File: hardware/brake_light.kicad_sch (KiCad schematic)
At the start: 4 parts, among them Q5 PMV450ENEA

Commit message: Add the Cube project
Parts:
- R?: Case 0603 -> (none)
- R?: value R_Small -> 10k
- R?: value R_Small -> 100R
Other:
- note removed: "TODO: Add a mosfet driver"
- moved on the sheet: Q5, R?
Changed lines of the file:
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@@
   (paper "A4")
   (title_block
-    (date "2023-06-06")
+    (date "2023-07-01")
     (rev "${REVISION}")
     (company "Author: I. Kajdan")
     (comment 1 "Reviewer:")
   )
-  (junction (at 153.67 100.33) (diameter 0) (color 0 0 0 0)
+  (junction (at 151.13 110.49) (diameter 0) (color 0 0 0 0)
   )
-  (junction (at 143.51 92.71) (diameter 0) (color 0 0 0 0)
+  (junction (at 140.97 102.87) (diameter 0) (color 0 0 0 0)
   )
-  (wire (pts (xy 135.89 92.71) (xy 133.35 92.71))
+  (wire (pts (xy 133.35 102.87) (xy 130.81 102.87))
     (stroke (width 0) (type default))
   )
-  (wire (pts (xy 153.67 104.14) (xy 153.67 100.33))
+  (wire (pts (xy 151.13 114.3) (xy 151.13 110.49))
     (stroke (width 0) (type default))
   )
-  (wire (pts (xy 143.51 100.33) (xy 146.05 100.33))
+  (wire (pts (xy 140.97 110.49) (xy 143.51 110.49))
     (stroke (width 0) (type default))
   )
-  (wire (pts (xy 143.51 100.33) (xy 143.51 92.71))
+  (wire (pts (xy 140.97 110.49) (xy 140.97 102.87))
     (stroke (width 0) (type default))
   )
-  (wire (pts (xy 140.97 92.71) (xy 143.51 92.71))
+  (wire (pts (xy 138.43 102.87) (xy 140.97 102.87))
     (stroke (width 0) (type default))
   )
-  (wire (pts (xy 153.67 100.33) (xy 153.67 97.79))
+  (wire (pts (xy 151.13 110.49) (xy 151.13 107.95))
     (stroke (width 0) (type default))
   )
-  (wire (pts (xy 153.67 83.82) (xy 153.67 87.63))
+  (wire (pts (xy 151.13 96.52) (xy 151.13 97.79))
     (stroke (width 0) (type default))
   )
-  (wire (pts (xy 143.51 92.71) (xy 146.05 92.71))
+  (wire (pts (xy 140.97 102.87) (xy 143.51 102.87))
     (stroke (width 0) (type default))
   )
-  (wire (pts (xy 153.67 74.93) (xy 153.67 78.74))
+  (wire (pts (xy 151.13 88.9) (xy 151.13 91.44))
     (stroke (width 0) (type default))
   )
-  (wire (pts (xy 151.13 100.33) (xy 153.67 100.33))
+  (wire (pts (xy 148.59 110.49) (xy 151.13 110.49))
     (stroke (width 0) (type default))
   )
-  (wire (pts (xy 157.48 74.93) (xy 153.67 74.93))
+  (wire (pts (xy 154.94 88.9) (xy 151.13 88.9))
     (stroke (width 0) (type default))
   )
-  (text "TODO: Add a mosfet driver" (at 139.7 124.46 0)
-    (effects (font (size 1.27 1.27)) (justify left bottom))
-  )
-  (hierarchical_label "OUT" (shape output) (at 157.48 74.93 0) (fields_autoplaced)
+  (hierarchical_label "OUT" (shape output) (at 154.94 88.9 0) (fields_autoplaced)
     (effects (font (size 1.27 1.27)) (justify left))
   )
-  (hierarchical_label "IN" (shape input) (at 133.35 92.71 180) (fields_autoplaced)
+  (hierarchical_label "IN" (shape input) (at 130.81 102.87 180) (fields_autoplaced)
     (effects (font (size 1.27 1.27)) (justify right))
   )
-  (symbol (lib_id "Simulation_SPICE:NMOS") (at 151.13 92.71 0) (unit 1)
+  (symbol (lib_id "Simulation_SPICE:NMOS") (at 148.59 102.87 0) (unit 1)
     (in_bom yes) (on_board yes) (dnp no)
-    (property "Reference" "Q5" (at 157.48 91.44 0)
+    (property "Reference" "Q5" (at 153.67 101.6 0)
       (effects (font (size 1.27 1.27)) (justify left))
     )
-    (property "Value" "PMV450ENEA" (at 157.48 93.98 0)
+    (property "Value" "PMV450ENEA" (at 153.67 104.14 0)
       (effects (font (size 1.27 1.27)) (justify left))
     )
-    (property "Footprint" "" (at 156.21 90.17 0)
+    (property "Footprint" "" (at 153.67 100.33 0)
       (effects (font (size 1.27 1.27)) hide)
     )
-    (property "Datasheet" "https://assets.nexperia.com/documents/data-sheet/PMV450ENEA.pdf" (at 151.13 105.41 0)
+    (property "Datasheet" "https://assets.nexperia.com/documents/data-sheet/PMV450ENEA.pdf" (at 148.59 115.57 0)
       (effects (font (size 1.27 1.27)) hide)
     )
@@
     )
   )
-  (symbol (lib_id "Device:R_Small") (at 153.67 81.28 0) (unit 1)
+  (symbol (lib_id "Device:R_Small") (at 151.13 93.98 0) (unit 1)
     (in_bom yes) (on_board yes) (dnp no)
-    (property "Reference" "R?" (at 156.4386 78.8416 0)
+    (property "Reference" "R?" (at 152.6286 92.8116 0)
       (effects (font (size 1.27 1.27)) (justify left))
     )
-    (property "Value" "0R" (at 156.4386 81.153 0)
+    (property "Value" "0R" (at 152.6286 95.123 0)
       (effects (font (size 1.27 1.27)) (justify left))
     )
-    (property "Footprint" "Resistor_SMD:R_0603_1608Metric" (at 153.67 81.28 0)
+    (property "Footprint" "Resistor_SMD:R_0603_1608Metric" (at 151.13 93.98 0)
       (effects (font (size 1.27 1.27)) hide)
     )
-    (property "Datasheet" "~" (at 153.67 81.28 0)
+    (property "Datasheet" "~" (at 151.13 93.98 0)
       (effects (font (size 1.27 1.27)) hide)
-    )
-    (property "Case" "0603" (at 156.4386 83.82 0)
-      (effects (font (size 1.27 1.27)) (justify left))
     )
     (pin "1")
@@
     )
   )
-  (symbol (lib_id "Device:R_Small") (at 148.59 100.33 270) (unit 1)
+  (symbol (lib_id "Device:R_Small") (at 146.05 110.49 270) (unit 1)
     (in_bom yes) (on_board yes) (dnp no)
-    (property "Reference" "R?" (at 148.59 97.79 90)
+    (property "Reference" "R?" (at 146.05 107.95 90)
       (effects (font (size 1.27 1.27)))
     )
-    (property "Value" "R_Small" (at 148.59 102.87 90)
+    (property "Value" "10k" (at 146.05 113.03 90)
       (effects (font (size 1.27 1.27)))
     )
-    (property "Footprint" "Resistor_SMD:R_0402_1005Metric" (at 148.59 100.33 0)
+    (property "Footprint" "Resistor_SMD:R_0402_1005Metric" (at 146.05 110.49 0)
       (effects (font (size 1.27 1.27)) hide)
     )
-    (property "Datasheet" "~" (at 148.59 100.33 0)
+    (property "Datasheet" "~" (at 146.05 110.49 0)
       (effects (font (size 1.27 1.27)) hide)
     )
@@
     )
   )
-  (symbol (lib_id "power:GND") (at 153.67 104.14 0) (unit 1)
+  (symbol (lib_id "power:GND") (at 151.13 114.3 0) (unit 1)
     (in_bom yes) (on_board yes) (dnp no)
-    (property "Reference" "#PWR?" (at 153.67 110.49 0)
+    (property "Reference" "#PWR?" (at 151.13 120.65 0)
       (effects (font (size 1.27 1.27)) hide)
     )
-    (property "Value" "GND" (at 153.797 108.5342 0)
+    (property "Value" "GND" (at 151.257 118.6942 0)
       (effects (font (size 1.27 1.27)))
     )
-    (property "Footprint" "" (at 153.67 104.14 0)
+    (property "Footprint" "" (at 151.13 114.3 0)
       (effects (font (size 1.27 1.27)) hide)
     )
-    (property "Datasheet" "" (at 153.67 104.14 0)
+    (property "Datasheet" "" (at 151.13 114.3 0)
       (effects (font (size 1.27 1.27)) hide)
     )
@@
     )
   )
-  (symbol (lib_id "Device:R_Small") (at 138.43 92.71 270) (unit 1)
+  (symbol (lib_id "Device:R_Small") (at 135.89 102.87 270) (unit 1)
     (in_bom yes) (on_board yes) (dnp no)
-    (property "Reference" "R?" (at 138.43 90.17 90)
+    (property "Reference" "R?" (at 135.89 100.33 90)
       (effects (font (size 1.27 1.27)))
     )
-    (property "Value" "R_Small" (at 142.113 95.0214 90)
+    (property "Value" "100R" (at 138.303 105.1814 90)
       (effects (font (size 1.27 1.27)) (justify right))
     )
-    (property "Footprint" "Resistor_SMD:R_0402_1005Metric" (at 138.43 92.71 0)
+    (property "Footprint" "Resistor_SMD:R_0402_1005Metric" (at 135.89 102.87 0)
       (effects (font (size 1.27 1.27)) hide)
     )
-    (property "Datasheet" "~" (at 138.43 92.71 0)
+    (property "Datasheet" "~" (at 135.89 102.87 0)
       (effects (font (size 1.27 1.27)) hide)
     )

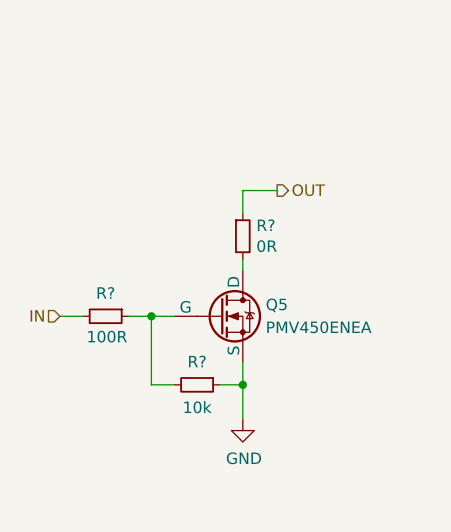
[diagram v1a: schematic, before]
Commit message: Improve the schematic
- add anti-aliasing filters
- rearrange the main connector signals
- improve the power filtering
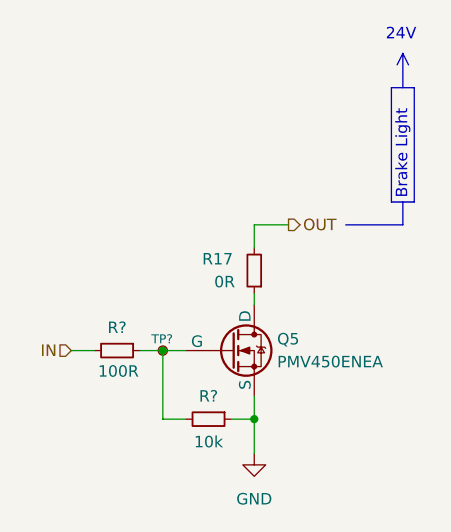
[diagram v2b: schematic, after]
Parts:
- removed R?: 0R, Resistor_SMD:R_0603_1608Metric, symbol Device:R_Small
- added R17: 0R, Resistor_SMD:R_0603_1608Metric, symbol Device:R_Small
- added TP?: TestPoint_Small, TestPoint:TestPoint_Pad_D1.0mm, symbol Connector:TestPoint_Small
- R? (x2): footprint Resistor_SMD:R_0402_1005Metric -> Resistor_SMD:R_0603_1608Metric
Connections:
- net OUT: now also R17.2
- net at Q5.1 (D): now also R17.1
- net at Q5.2 (G), R?.1, R?.2: now also TP?.1
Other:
- note added: "24V"
- note added: "Brake Light"
- moved on the sheet: Q5, R?

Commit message: Set component values
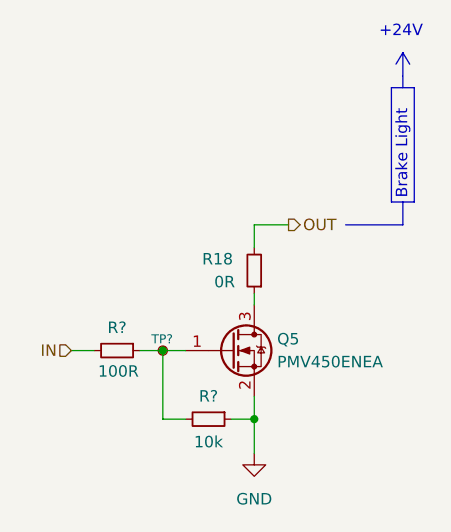
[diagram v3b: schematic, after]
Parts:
- Q5: symbol Simulation_SPICE:NMOS -> Device:Q_NMOS_GSD
- renumbered R17 to R18
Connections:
- net GND: now also Q5.2 (S); no longer Q5.3 (S)
- net at Q5.1 (G): now also R?.1, R?.2, TP?.1; no longer R18.1
- new net: Q5.3 (D), R18.1
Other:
- note added: "+24V"
- note removed: "24V"
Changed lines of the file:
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@@
     (stroke (width 0) (type default))
   )
-  (polyline (pts (xy 168.91 73.66) (xy 168.91 77.47))
+  (polyline (pts (xy 168.148 74.8538) (xy 168.91 73.5838))
     (stroke (width 0) (type default))
   )
@@
     (stroke (width 0) (type default))
   )
+  (polyline (pts (xy 168.91 73.5838) (xy 168.91 76.1492))
+    (stroke (width 0) (type default))
+  )
   (wire (pts (xy 142.24 114.3) (xy 142.24 106.68))
     (stroke (width 0) (type default))
   )
-  (polyline (pts (xy 168.275 74.93) (xy 168.91 73.66))
-    (stroke (width 0) (type default))
-  )
   (wire (pts (xy 139.7 106.68) (xy 142.24 106.68))
     (stroke (width 0) (type default))
@@
     (stroke (width 0) (type default))
   )
+  (polyline (pts (xy 169.672 74.8538) (xy 168.91 73.5838))
+    (stroke (width 0) (type default))
+  )
+  (polyline (pts (xy 168.91 76.2) (xy 168.91 77.47))
+    (stroke (width 0) (type default))
+  )
   (wire (pts (xy 142.24 106.68) (xy 144.78 106.68))
     (stroke (width 0) (type default))
@@
     (stroke (width 0) (type default))
   )
-  (polyline (pts (xy 168.91 73.66) (xy 169.545 74.93))
-    (stroke (width 0) (type default))
-  )
   (wire (pts (xy 156.21 92.71) (xy 152.4 92.71))
     (stroke (width 0) (type default))
-  )
-  (text "24V" (at 167.005 72.39 0)
-    (effects (font (size 1.27 1.27)) (justify left bottom))
   )
   (text "Brake Light" (at 169.545 89.916 90)
     (effects (font (size 1.27 1.27)) (justify left bottom))
   )
+  (text "+24V" (at 166.2684 72.0344 0)
+    (effects (font (size 1.27 1.27)) (justify left bottom))
+  )
   (hierarchical_label "OUT" (shape output) (at 156.21 92.71 0) (fields_autoplaced)
     (effects (font (size 1.27 1.27)) (justify left))
@@
     (effects (font (size 1.27 1.27)) (justify right))
   )
-  (symbol (lib_id "Simulation_SPICE:NMOS") (at 149.86 106.68 0) (unit 1)
+  (symbol (lib_id "Device:Q_NMOS_GSD") (at 149.86 106.68 0) (unit 1)
     (in_bom yes) (on_board yes) (dnp no)
     (property "Reference" "Q5" (at 154.94 105.41 0)
@@
       (effects (font (size 1.27 1.27)) hide)
     )
-    (property "Datasheet" "https://assets.nexperia.com/documents/data-sheet/PMV450ENEA.pdf" (at 149.86 119.38 0)
+    (property "Datasheet" "~" (at 149.86 106.68 0)
       (effects (font (size 1.27 1.27)) hide)
     )
@@
         )
         (path "/b652b05a-4e3d-4ad1-b032-18886abe7d45/91248db3-ac16-4fb7-9cfe-25145bb94249"
-          (reference "R16") (unit 1)
+          (reference "R17") (unit 1)
         )
       )
@@
   (symbol (lib_id "Device:R_Small") (at 152.4 97.79 180) (unit 1)
     (in_bom yes) (on_board yes) (dnp no)
-    (property "Reference" "R17" (at 150.0378 96.52 0)
+    (property "Reference" "R18" (at 150.0378 96.52 0)
       (effects (font (size 1.27 1.27)) (justify left))
     )
@@
       (project "rearbox"
         (path "/b652b05a-4e3d-4ad1-b032-18886abe7d45/91248db3-ac16-4fb7-9cfe-25145bb94249"
-          (reference "R17") (unit 1)
+          (reference "R18") (unit 1)
         )
         (path "/b652b05a-4e3d-4ad1-b032-18886abe7d45"
@@
         )
         (path "/b652b05a-4e3d-4ad1-b032-18886abe7d45/91248db3-ac16-4fb7-9cfe-25145bb94249"
-          (reference "R15") (unit 1)
-        )
-      )
+          (reference "R16") (unit 1)
+        )
+      )

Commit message: Improve the schematic according to the feedback
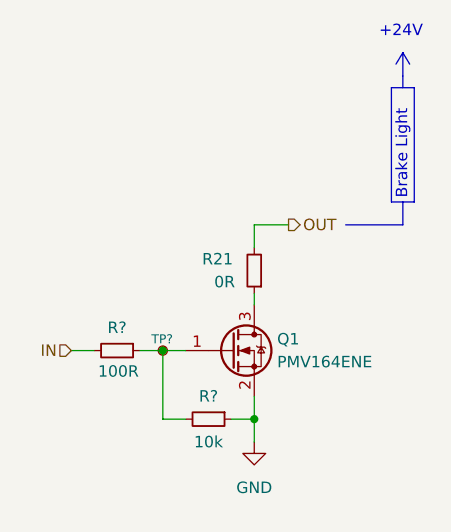
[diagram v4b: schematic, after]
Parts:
- Q1: renamed from Q5; value PMV450ENEA -> PMV164ENE; footprint (none) -> Package_TO_SOT_SMD:SOT-23
- renumbered R18 to R21
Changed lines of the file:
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@@
     (stroke (width 0) (type default))
   )
-  (wire (pts (xy 152.4 118.11) (xy 152.4 114.3))
+  (wire (pts (xy 152.4 116.84) (xy 152.4 114.3))
     (stroke (width 0) (type default))
   )
@@
   (symbol (lib_id "Device:Q_NMOS_GSD") (at 149.86 106.68 0) (unit 1)
     (in_bom yes) (on_board yes) (dnp no)
-    (property "Reference" "Q5" (at 154.94 105.41 0)
-      (effects (font (size 1.27 1.27)) (justify left))
-    )
-    (property "Value" "PMV450ENEA" (at 154.94 107.95 0)
-      (effects (font (size 1.27 1.27)) (justify left))
-    )
-    (property "Footprint" "" (at 154.94 104.14 0)
-      (effects (font (size 1.27 1.27)) hide)
-    )
-    (property "Datasheet" "~" (at 149.86 106.68 0)
+    (property "Reference" "Q1" (at 154.94 105.41 0)
+      (effects (font (size 1.27 1.27)) (justify left))
+    )
+    (property "Value" "PMV164ENE" (at 154.94 107.95 0)
+      (effects (font (size 1.27 1.27)) (justify left))
+    )
+    (property "Footprint" "Package_TO_SOT_SMD:SOT-23" (at 154.94 104.14 0)
+      (effects (font (size 1.27 1.27)) hide)
+    )
+    (property "Datasheet" "https://www.mouser.pl/datasheet/2/916/PMV164ENE-2909806.pdf" (at 149.86 106.68 0)
       (effects (font (size 1.27 1.27)) hide)
     )
@@
       (project "rearbox"
         (path "/b652b05a-4e3d-4ad1-b032-18886abe7d45/91248db3-ac16-4fb7-9cfe-25145bb94249"
-          (reference "Q5") (unit 1)
-        )
-      )
-    )
-  )
-  (symbol (lib_id "power:GND") (at 152.4 118.11 0) (unit 1)
+          (reference "Q1") (unit 1)
+        )
+      )
+    )
+  )
+  (symbol (lib_id "power:GND") (at 152.4 116.84 0) (unit 1)
     (in_bom yes) (on_board yes) (dnp no) (fields_autoplaced)
-    (property "Reference" "#PWR022" (at 152.4 124.46 0)
-      (effects (font (size 1.27 1.27)) hide)
-    )
-    (property "Value" "GND" (at 152.4 123.19 0)
-      (effects (font (size 1.27 1.27)))
-    )
-    (property "Footprint" "" (at 152.4 118.11 0)
-      (effects (font (size 1.27 1.27)) hide)
-    )
-    (property "Datasheet" "" (at 152.4 118.11 0)
-      (effects (font (size 1.27 1.27)) hide)
-    )
-    (pin "1")
-    (instances
-      (project "rearbox"
-        (path "/b652b05a-4e3d-4ad1-b032-18886abe7d45/91248db3-ac16-4fb7-9cfe-25145bb94249"
-          (reference "#PWR022") (unit 1)
+    (property "Reference" "#PWR066" (at 152.4 123.19 0)
+      (effects (font (size 1.27 1.27)) hide)
+    )
+    (property "Value" "GND" (at 152.4 121.92 0)
+      (effects (font (size 1.27 1.27)))
+    )
+    (property "Footprint" "" (at 152.4 116.84 0)
+      (effects (font (size 1.27 1.27)) hide)
+    )
+    (property "Datasheet" "" (at 152.4 116.84 0)
+      (effects (font (size 1.27 1.27)) hide)
+    )
+    (pin "1")
+    (instances
+      (project "rearbox"
+        (path "/b652b05a-4e3d-4ad1-b032-18886abe7d45/91248db3-ac16-4fb7-9cfe-25145bb94249"
+          (reference "#PWR066") (unit 1)
         )
       )
@@
         )
         (path "/b652b05a-4e3d-4ad1-b032-18886abe7d45/91248db3-ac16-4fb7-9cfe-25145bb94249"
-          (reference "R17") (unit 1)
+          (reference "R20") (unit 1)
         )
       )
@@
   (symbol (lib_id "Device:R_Small") (at 152.4 97.79 180) (unit 1)
     (in_bom yes) (on_board yes) (dnp no)
-    (property "Reference" "R18" (at 150.0378 96.52 0)
+    (property "Reference" "R21" (at 150.0378 96.52 0)
       (effects (font (size 1.27 1.27)) (justify left))
     )
@@
       (project "rearbox"
         (path "/b652b05a-4e3d-4ad1-b032-18886abe7d45/91248db3-ac16-4fb7-9cfe-25145bb94249"
-          (reference "R18") (unit 1)
+          (reference "R21") (unit 1)
         )
         (path "/b652b05a-4e3d-4ad1-b032-18886abe7d45"
@@
         )
         (path "/b652b05a-4e3d-4ad1-b032-18886abe7d45/91248db3-ac16-4fb7-9cfe-25145bb94249"
-          (reference "TP7") (unit 1)
+          (reference "TP14") (unit 1)
         )
       )
@@
         )
         (path "/b652b05a-4e3d-4ad1-b032-18886abe7d45/91248db3-ac16-4fb7-9cfe-25145bb94249"
-          (reference "R16") (unit 1)
-        )
-      )
+          (reference "R19") (unit 1)
+        )
+      )

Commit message: Add high-side drivers to the fans and pumps
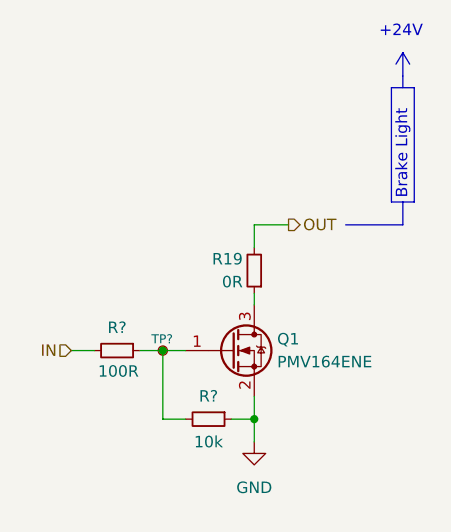
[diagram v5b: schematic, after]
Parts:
- renumbered R21 to R19
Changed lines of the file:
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@@
   (paper "A4")
   (title_block
-    (date "2023-07-01")
+    (date "2023-09-20")
     (rev "${REVISION}")
     (company "Author: I. Kajdan")
@@
   (symbol (lib_id "power:GND") (at 152.4 116.84 0) (unit 1)
     (in_bom yes) (on_board yes) (dnp no) (fields_autoplaced)
-    (property "Reference" "#PWR066" (at 152.4 123.19 0)
+    (property "Reference" "#PWR067" (at 152.4 123.19 0)
       (effects (font (size 1.27 1.27)) hide)
     )
@@
       (project "rearbox"
         (path "/b652b05a-4e3d-4ad1-b032-18886abe7d45/91248db3-ac16-4fb7-9cfe-25145bb94249"
-          (reference "#PWR066") (unit 1)
+          (reference "#PWR067") (unit 1)
         )
       )
@@
         )
         (path "/b652b05a-4e3d-4ad1-b032-18886abe7d45/91248db3-ac16-4fb7-9cfe-25145bb94249"
-          (reference "R20") (unit 1)
+          (reference "R18") (unit 1)
         )
       )
@@
   (symbol (lib_id "Device:R_Small") (at 152.4 97.79 180) (unit 1)
     (in_bom yes) (on_board yes) (dnp no)
-    (property "Reference" "R21" (at 150.0378 96.52 0)
-      (effects (font (size 1.27 1.27)) (justify left))
-    )
-    (property "Value" "0R" (at 150.2664 99.06 0)
+    (property "Reference" "R19" (at 151.13 96.52 0)
+      (effects (font (size 1.27 1.27)) (justify left))
+    )
+    (property "Value" "0R" (at 151.13 99.06 0)
       (effects (font (size 1.27 1.27)) (justify left))
     )
@@
       (project "rearbox"
         (path "/b652b05a-4e3d-4ad1-b032-18886abe7d45/91248db3-ac16-4fb7-9cfe-25145bb94249"
-          (reference "R21") (unit 1)
+          (reference "R19") (unit 1)
         )
         (path "/b652b05a-4e3d-4ad1-b032-18886abe7d45"
@@
         )
         (path "/b652b05a-4e3d-4ad1-b032-18886abe7d45/91248db3-ac16-4fb7-9cfe-25145bb94249"
-          (reference "R19") (unit 1)
-        )
-      )
+          (reference "R17") (unit 1)
+        )
+      )

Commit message: Improve the diagram based on the feedback
- add an input LC filter
- remove the USB connector
- add a programmer connector
- move optocouplers into a subsheet
- add a suspension tension meter IC
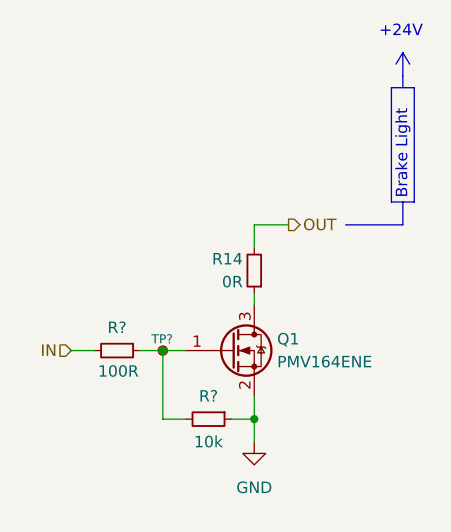
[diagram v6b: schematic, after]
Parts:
- renumbered R19 to R14
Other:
- title: (none) -> Brake Light
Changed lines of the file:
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@@
   (paper "A4")
   (title_block
-    (date "2023-09-20")
+    (title "Brake Light")
+    (date "2023-10-01")
     (rev "${REVISION}")
     (company "Author: I. Kajdan")
@@
   (symbol (lib_id "power:GND") (at 152.4 116.84 0) (unit 1)
     (in_bom yes) (on_board yes) (dnp no) (fields_autoplaced)
-    (property "Reference" "#PWR067" (at 152.4 123.19 0)
+    (property "Reference" "#PWR070" (at 152.4 123.19 0)
       (effects (font (size 1.27 1.27)) hide)
     )
@@
       (project "rearbox"
         (path "/b652b05a-4e3d-4ad1-b032-18886abe7d45/91248db3-ac16-4fb7-9cfe-25145bb94249"
-          (reference "#PWR067") (unit 1)
+          (reference "#PWR070") (unit 1)
         )
       )
@@
         )
         (path "/b652b05a-4e3d-4ad1-b032-18886abe7d45/91248db3-ac16-4fb7-9cfe-25145bb94249"
-          (reference "R18") (unit 1)
+          (reference "R13") (unit 1)
         )
       )
@@
   (symbol (lib_id "Device:R_Small") (at 152.4 97.79 180) (unit 1)
     (in_bom yes) (on_board yes) (dnp no)
-    (property "Reference" "R19" (at 151.13 96.52 0)
+    (property "Reference" "R14" (at 151.13 96.52 0)
       (effects (font (size 1.27 1.27)) (justify left))
     )
@@
       (project "rearbox"
         (path "/b652b05a-4e3d-4ad1-b032-18886abe7d45/91248db3-ac16-4fb7-9cfe-25145bb94249"
-          (reference "R19") (unit 1)
+          (reference "R14") (unit 1)
         )
         (path "/b652b05a-4e3d-4ad1-b032-18886abe7d45"
@@
         )
         (path "/b652b05a-4e3d-4ad1-b032-18886abe7d45/91248db3-ac16-4fb7-9cfe-25145bb94249"
-          (reference "TP14") (unit 1)
+          (reference "TP15") (unit 1)
         )
       )
@@
         )
         (path "/b652b05a-4e3d-4ad1-b032-18886abe7d45/91248db3-ac16-4fb7-9cfe-25145bb94249"
-          (reference "R17") (unit 1)
-        )
-      )
+          (reference "R12") (unit 1)
+        )
+      )
